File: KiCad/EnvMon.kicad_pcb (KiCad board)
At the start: 2 copper layers, 44.5 x 37 mm, 14 parts, among them J1 DS18B20, J2 Prog, J3 12V, J4 USB-C, M1 SCD30, M2 OLED1.5-I2C, M3 D24V5F3, SW1 GPIO0, U1 ESP32-WROOM-32

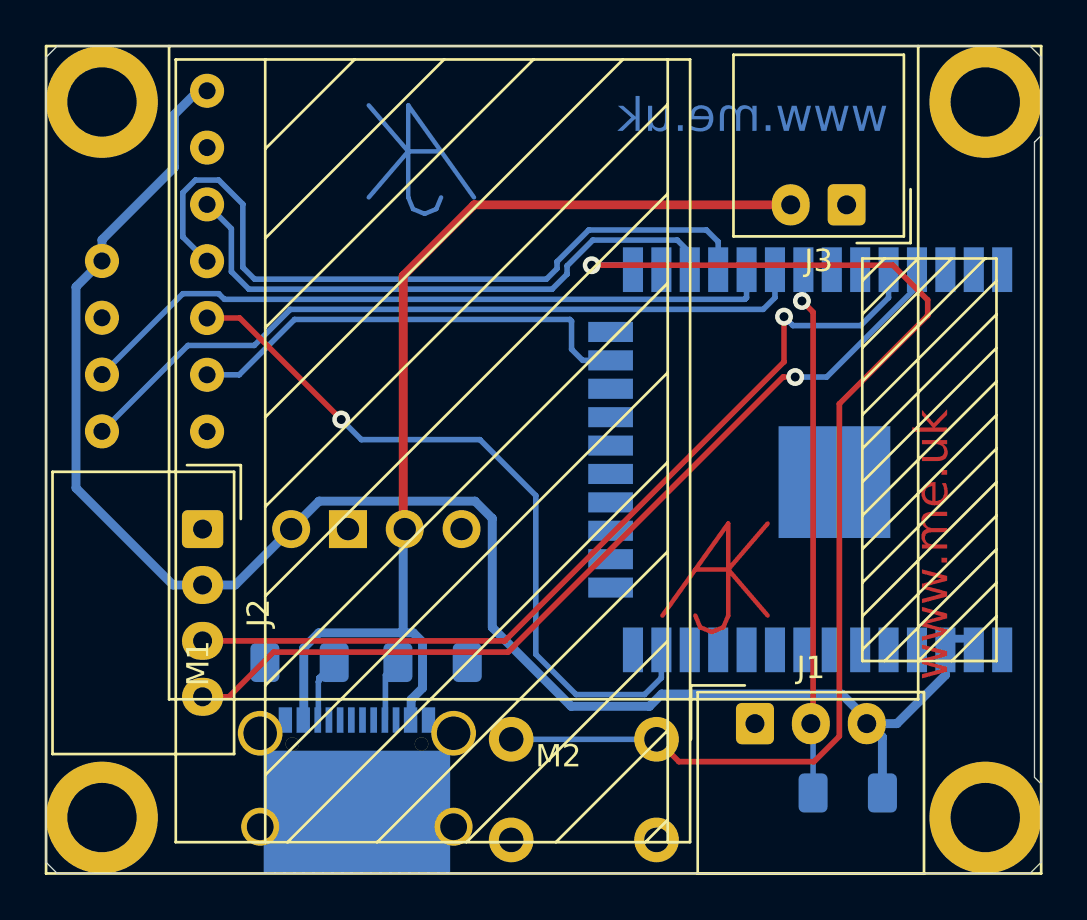
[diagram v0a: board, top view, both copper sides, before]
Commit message: Corrected tx/rx
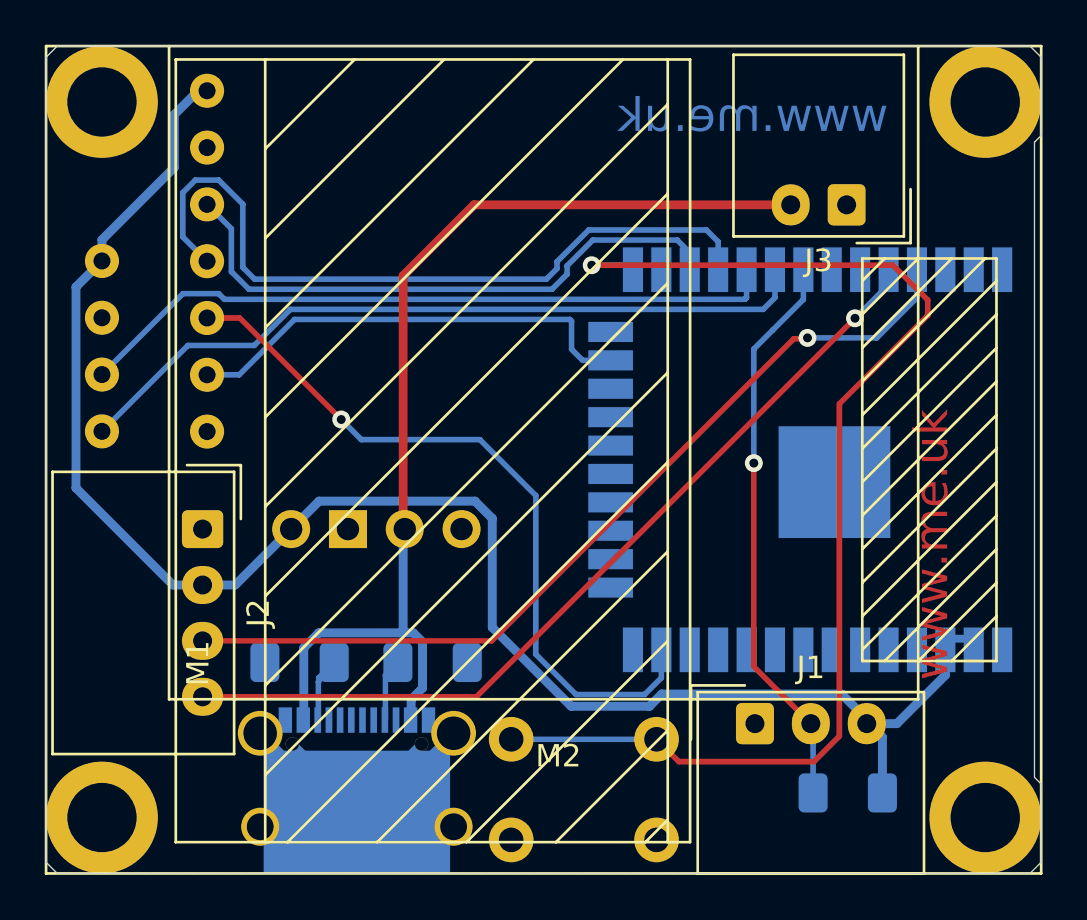
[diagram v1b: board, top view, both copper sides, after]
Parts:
- removed REF** (x2): AJK, RevK:AJK
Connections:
- U1 pad 34: Net-(J2-Pad3) -> Net-(J2-Pad4)
- U1 pad 35: Net-(J2-Pad4) -> Net-(J2-Pad3)
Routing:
- net GND: track 2.74 -> 31.8 mm
- net /TEMP: track 24.1 -> 25.9 mm
- net Net-(J2-Pad4): track 40.7 -> 39.0 mm

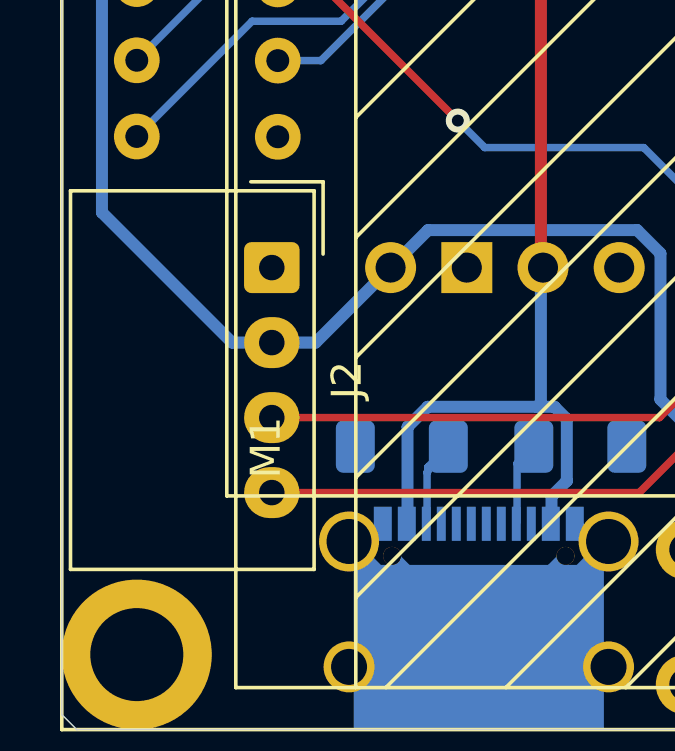
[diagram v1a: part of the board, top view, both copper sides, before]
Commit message: Tidied schematic diagrams
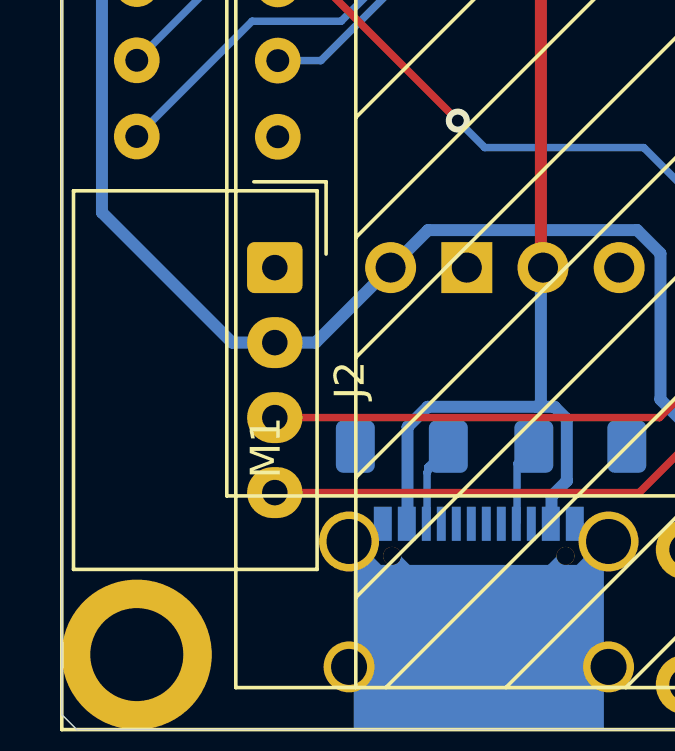
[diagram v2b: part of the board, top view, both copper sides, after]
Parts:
- moved J2 0.10 mm to (127.0, 100.0)
